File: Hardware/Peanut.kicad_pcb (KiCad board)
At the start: 2 copper layers, 58 x 36 mm, 42 parts, among them J1 Conn_02x04_Odd_Even, J2 Conn_02x04_Odd_Even, SW1 Push_Button, SW2 Push_Button, SW3 Push_Button, SW4 Push_Button, SW5 Slide Switch, U1 BNO085, U2 PCF8574, U3 HDC2010YPAR, U4 LTR-303ALS-01, U5 ADS1115IDGSR, Y1 Crystal_32.768kHz

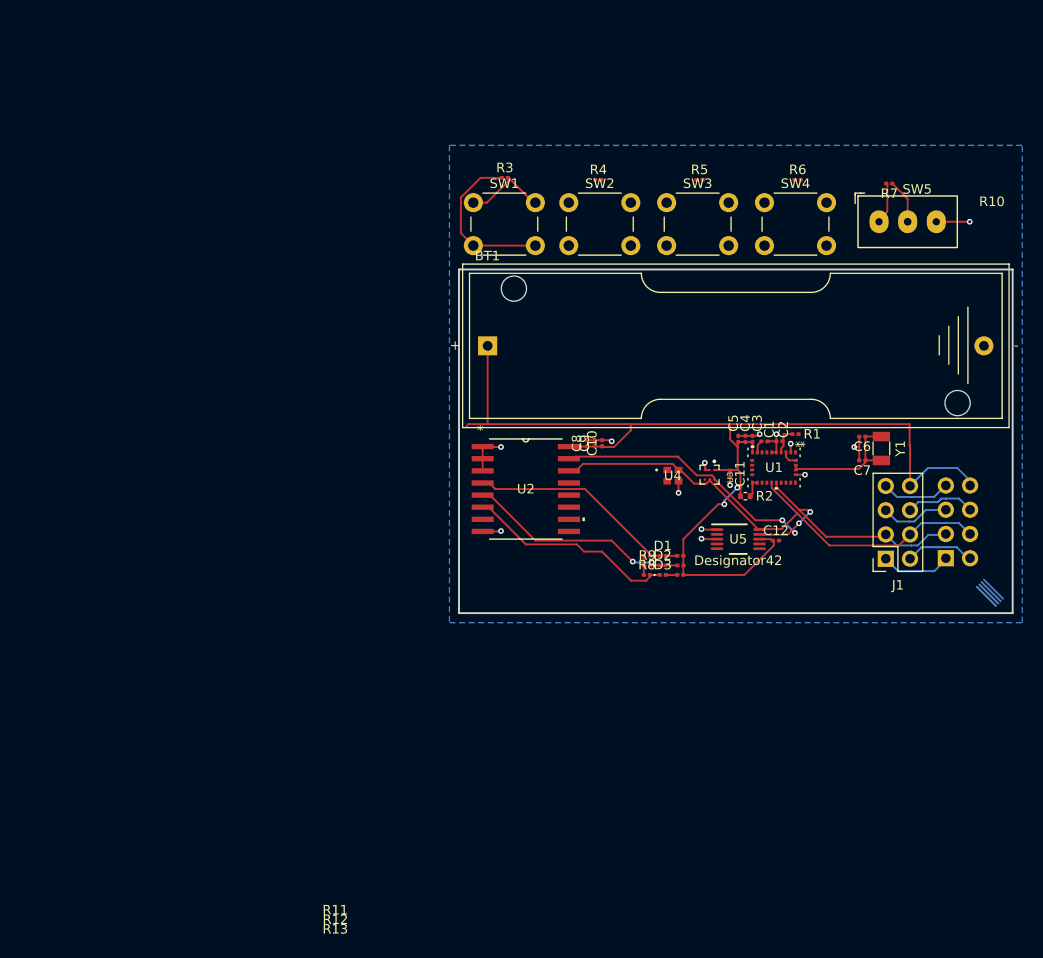
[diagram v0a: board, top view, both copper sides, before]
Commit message: Use Peanut symbols, fix ERC errors, progress on DAC & Pressure
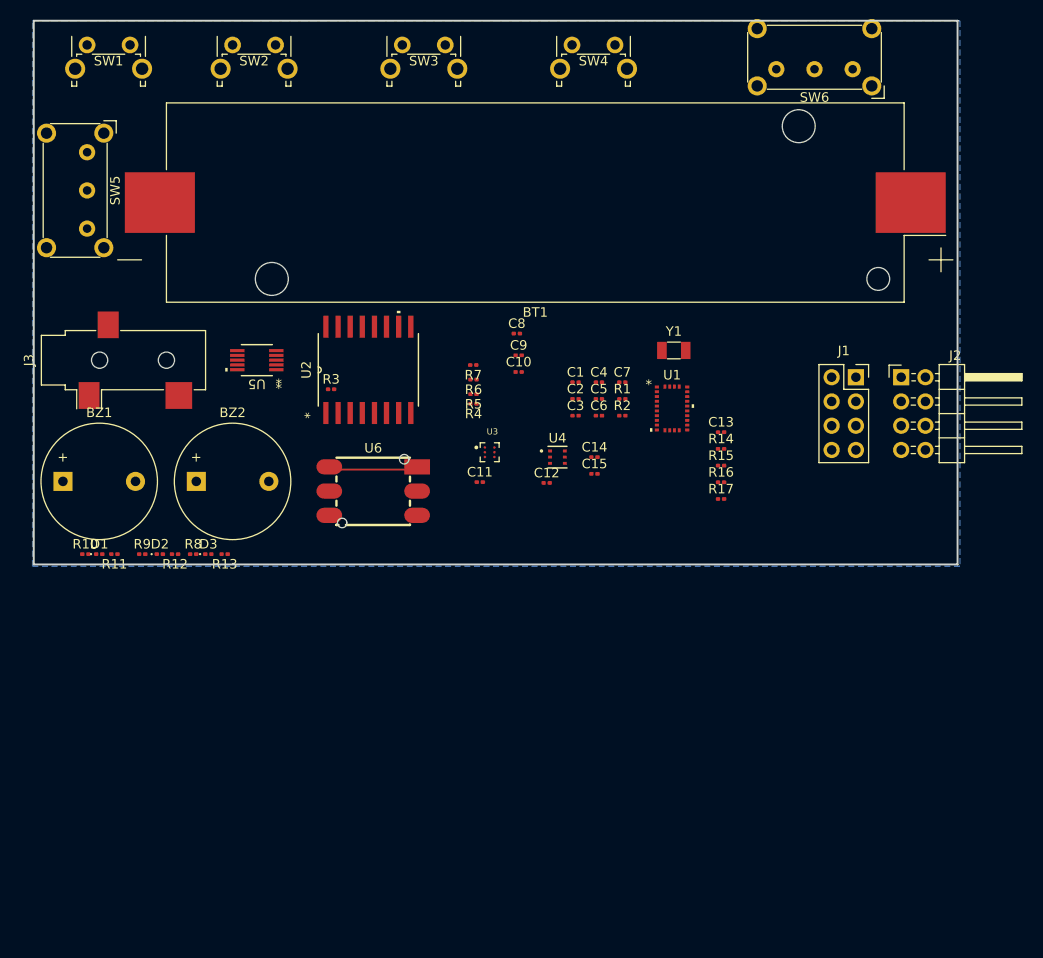
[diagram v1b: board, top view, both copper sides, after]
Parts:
- added BZ1: Buzzer, Buzzer_Beeper:Buzzer_12x9.5RM7.6, F.Cu at (63.5, 76.2)
- added BZ2: Buzzer, Buzzer_Beeper:Buzzer_12x9.5RM7.6, F.Cu at (77.5, 76.2)
- added C13: 0.1uF, Capacitor_SMD:C_0201_0603Metric, F.Cu at (132.5, 71.0)
- added C14: 0.1uF, Capacitor_SMD:C_0201_0603Metric, F.Cu at (119.2, 73.7)
- added C15: 0.1uF, Capacitor_SMD:C_0201_0603Metric, F.Cu at (119.2, 75.4)
- added J3: AudioPlug3, Connector_Audio:Jack_3.5mm_CUI_SJ-3523-SMT_Horizontal, F.Cu at (69.8, 63.5)
- added R14: 1k, Resistor_SMD:R_0201_0603Metric, F.Cu at (132.5, 72.8)
- added R15: 1k, Resistor_SMD:R_0201_0603Metric, F.Cu at (132.5, 74.5)
- added R16: 56k, Resistor_SMD:R_0201_0603Metric, F.Cu at (132.5, 76.3)
- added R17: 56k, Resistor_SMD:R_0201_0603Metric, F.Cu at (132.5, 78.0)
- added SW6: Slide Switch, Button_Switch_THT:SW_E-Switch_EG1224_SPDT_Angled, F.Cu at (146.2, 33.0)
- added U6: LWP040-PSGLC-S, Peanut:SOP-4_L7.0-W7.0-P2.54-LS10.3-TL-CW_LWP040-PSGLC-S, F.Cu at (96.0, 77.2)
- BT1: value Battery -> 3.3V; footprint Battery:BatteryHolder_Keystone_2460_1xAA -> Battery:BatteryHolder_Keystone_1042_1x18650
- J2: moved to F.Cu
- R2: footprint Resistor_SMD:R_0402_1005Metric -> Resistor_SMD:R_0201_0603Metric
- SW1, SW2, SW3, SW4: footprint Button_Switch_THT:SW_PUSH_6mm -> Button_Switch_THT:SW_Tactile_SPST_Angled_PTS645Vx58-2LFS
- SW5: footprint PCM_SL_Devices:Slide_Switch_SPDT_P3mm_10x5x10mm -> Button_Switch_THT:SW_E-Switch_EG1224_SPDT_Angled
- U1: footprint Snapeda:LGA28_5.2X3.8_CEV -> Peanut:LGA28_5.2X3.8_CEV
- U2: footprint Snapeda:DW16 -> Peanut:DW16
- U3: footprint Snapeda:BGA6C100X50P2X3_HDC2010YPAR -> Peanut:HDC2010YPAR
- U4: footprint Snapeda:LTR-329ALS-01_LTO -> Peanut:LTR-308ALS-01_LTO
- U5: value ADS1115IDGSR -> MCP4728T-E/UN; footprint Snapeda:DGS0010A_N -> Peanut:MSOP10_MC_MCH
- moved SW5 83.3 mm to (66.0, 41.7), turned to -90 degrees
- moved R11 59.3 mm to (68.9, 83.8)
- moved D1 59.0 mm to (67.3, 83.8)
- moved R10 58.8 mm to (65.9, 83.8)
- moved U5 53.8 mm to (83.8, 63.5), turned to 180 degrees
- moved R12 53.0 mm to (75.2, 83.8)
- moved R9 52.9 mm to (71.8, 83.8)
- moved D2 52.7 mm to (73.7, 83.8)
- moved R13 47.8 mm to (80.5, 83.8)
- moved D3 47.7 mm to (78.7, 83.8)
- moved R8 47.6 mm to (77.2, 83.8)
- moved R7 47.6 mm to (106.5, 64.0)
- moved SW1 43.7 mm to (66.0, 30.5)
- moved R6 39.9 mm to (106.5, 65.5), turned to 180 degrees
- moved SW2 38.9 mm to (81.3, 30.5)
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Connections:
- BT1 pad 1: +3V3 -> Net-(BT1-+)
- BT1 pad 2: GNDREF -> GND
- C1 pad 2: GNDREF -> GND
- C10 pad 2: GNDREF -> GND
- C11 pad 2: GNDREF -> GND
- C2 pad 1: GNDREF -> GND
- C3 pad 2: GNDREF -> GND
- C4 pad 2: GNDREF -> GND
- C5 pad 2: GNDREF -> GND
- C6 pad 2: GNDREF -> GND
- C7 pad 1: Net-(U1-XIN32) -> Net-(U1-XOUT32/CLKSEL1)
- C7 pad 2: GNDREF -> GND
- C8 pad 2: GNDREF -> GND
- C9 pad 2: GNDREF -> GND
- R3 pad 1: Net-(R3-Pad1) -> +3V3
- R4 pad 1: Net-(R3-Pad1) -> +3V3
- R5 pad 1: Net-(R3-Pad1) -> +3V3
- R6 pad 1: Net-(R3-Pad1) -> +3V3
- R7 pad 1: Net-(R3-Pad1) -> +3V3
- SW1 pad 2: Net-(R3-Pad1) -> +3V3
- SW2 pad 2: Net-(R3-Pad1) -> +3V3
- SW3 pad 2: Net-(R3-Pad1) -> +3V3
- SW4 pad 2: Net-(R3-Pad1) -> +3V3
- SW5 pad 2: Net-(R3-Pad1) -> +3V3
- SW5 pad 3: GNDREF -> GND
- U1 pad 2: GNDREF -> GND
- U1 pad 25: GNDREF -> GND
- U1 pad 26: Net-(U1-XIN32) -> Net-(U1-XOUT32/CLKSEL1)
- U1 pad 5: GNDREF -> GND
- U1 pad 6: GNDREF -> GND
- U2 pad 1: GNDREF -> GND
- U2 pad 2: GNDREF -> GND
- U2 pad 3: GNDREF -> GND
- U2 pad 8: GNDREF -> GND
- U3 pad B1: GNDREF -> GND
- U3 pad C1: GNDREF -> GND
- U4 pad 3: GNDREF -> GND
- U5 pad 1: GNDREF -> +3V3
- U5 pad 10: SCL -> GND
- U5 pad 2: unconnected-(U5-ALERT_RDY-Pad2) -> SCL
- U5 pad 3: GNDREF -> SDA
- U5 pad 4: unconnected-(U5-AIN0-Pad4) -> GND
- U5 pad 6: unconnected-(U5-AIN2-Pad6) -> Net-(U5-VOUTA)
- U5 pad 7: unconnected-(U5-AIN3-Pad7) -> Net-(U5-VOUTB)
- U5 pad 8: +3V3 -> Net-(BZ2-+)
- U5 pad 9: SDA -> Net-(BZ1-+)
- Y1 pad 2: Net-(U1-XIN32) -> Net-(U1-XOUT32/CLKSEL1)
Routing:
- net +3V3: track 119.9 -> 0.00 mm, vias 2 -> 0
- net SDA: track 55.5 -> 0.00 mm, vias 4 -> 0
- net SCL: track 52.9 -> 0.00 mm
- net GNDREF: track 30.3 -> 0.00 mm, vias 14 -> 0
- net Net-(R3-Pad1): track 21.9 -> 0.00 mm
- net Net-(D3-K): track 21.8 -> 0.00 mm
- net Net-(D2-K): track 21.2 -> 0.00 mm, vias 2 -> 0
- net Net-(D1-K): track 21.1 -> 0.00 mm
- net Net-(U1-XIN32): track 14.3 -> 0.00 mm
- net (no net): track 11.3 -> 0.00 mm
- net Net-(U2-P3): track 9.24 -> 0.00 mm
- net Net-(J1-Pin_6): track 7.35 -> 0.00 mm
- net UART_TX: track 7.30 -> 0.00 mm
- net UART_RX: track 7.28 -> 0.00 mm
- net Net-(J1-Pin_5): track 7.08 -> 0.00 mm
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- added copper zone on B.Cu, net GND
- removed copper zone on B.Cu, net GNDREF
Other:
- board size 58 x 36 mm -> 96.8 x 57 mm

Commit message: Fully wired board!
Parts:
- removed D3: BLU, LED_SMD:LED_0201_0603Metric
- removed R13: 2.2k, Resistor_SMD:R_0201_0603Metric
- removed R16, R17: 56k, Resistor_SMD:R_0201_0603Metric
- removed R8: 100k, Resistor_SMD:R_0201_0603Metric
- added C16: 0.1uF, Resistor_SMD:R_01005_0402Metric, F.Cu at (156.5, 86.0)
- added C17: 0.1uF, Resistor_SMD:R_01005_0402Metric, F.Cu at (164.0, 86.0)
- added Q1: Q_NPN_BEC, Package_TO_SOT_SMD:SOT-23-3, F.Cu at (167.5, 78.0)
- added U7: ADS1015IDGSR, Package_SO:VSSOP-10_3x3mm_P0.5mm, F.Cu at (160.0, 85.5)
- added U8: INA350ABSIDDFR, Package_TO_SOT_SMD:TSOT-23-8, F.Cu at (154.0, 86.5)
- C1, C10, C11, C12, C14, C15, C2, C3, C4, C5, C8, C9: footprint Capacitor_SMD:C_0201_0603Metric -> Resistor_SMD:R_01005_0402Metric
- C13: value 0.1uF -> 1uF; footprint Capacitor_SMD:C_0201_0603Metric -> Resistor_SMD:R_01005_0402Metric
- J2: footprint Connector_PinHeader_2.54mm:PinHeader_2x04_P2.54mm_Horizontal -> Peanut:PinHeader_2x04_P2.54mm_Horizontal_Flipped; moved to B.Cu
- R1, R10, R11, R12, R2, R3, R4, R5, R6, R7, R9: footprint Resistor_SMD:R_0201_0603Metric -> Resistor_SMD:R_0402_1005Metric
- R14, R15: value 1k -> R; footprint Resistor_SMD:R_0201_0603Metric -> Resistor_SMD:R_0402_1005Metric
- SW5, SW6: footprint Button_Switch_THT:SW_E-Switch_EG1224_SPDT_Angled -> Peanut:SW-TH_SK12D07VG4
- U2: value PCF8574 -> PCF8574APWR; footprint Peanut:DW16 -> Peanut:PW20
- moved U2 71.2 mm to (165.0, 49.0), turned to 180 degrees
- moved C10 59.8 mm to (169.7, 52.0)
- moved C9 59.8 mm to (169.7, 50.5)
- moved C8 59.7 mm to (169.7, 49.5)
- moved BZ1 56.4 mm to (119.7, 81.0)
- moved BZ2 55.4 mm to (132.7, 81.0)
- moved U6 51.7 mm to (147.5, 82.0), turned to 90 degrees
- moved C11 49.1 mm to (146.3, 46.5), turned to 180 degrees
- moved R6 46.6 mm to (149.5, 47.5), turned to 90 degrees
- moved U3 45.7 mm to (147.0, 49.0)
- moved SW1 45.3 mm to (107.7, 48.2)
- moved SW2 45.1 mm to (122.7, 48.2)
- moved C6 44.0 mm to (163.2, 76.2), turned to 180 degrees
- moved C7 43.9 mm to (163.2, 81.2), turned to 180 degrees
- moved C1 43.6 mm to (159.5, 76.2)
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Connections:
- C13 pad 1: GND -> +3V3
- C13 pad 2: /Pressure and ADC/PRESSURE -> GND
- R14 pad 1: Net-(U6-VOUT+) -> Net-(Q1-E)
- R14 pad 2: Net-(U7--) -> Net-(U7-AIN3)
- R15 pad 1: Net-(U7-+) -> Net-(U7-AIN3)
- R15 pad 2: Net-(U6-VOUT-) -> GND
- R3 pad 2: Net-(U2-P3) -> Net-(U2-P4)
- R4 pad 2: Net-(U2-P4) -> Net-(U2-P3)
- R5 pad 2: Net-(U2-P5) -> Net-(U2-P1)
- R6 pad 2: Net-(U2-P6) -> Net-(U2-P2)
- R7 pad 2: Net-(U2-P7) -> Net-(U2-P5)
- SW1 pad 1: Net-(U2-P3) -> Net-(U2-P4)
- SW2 pad 1: Net-(U2-P4) -> Net-(U2-P3)
- SW3 pad 1: Net-(U2-P5) -> Net-(U2-P1)
- SW4 pad 1: Net-(U2-P6) -> +3V3
- SW4 pad 2: +3V3 -> Net-(U2-P2)
- SW5 pad 1: Net-(U2-P7) -> Net-(U2-P5)
- U1 pad 17: /Motion Sensor/I2CADDR -> GND
- U2 pad 1: GND -> /DigitalMuxer/~{INT}
- U2 pad 10: Net-(U2-P5) -> /DigitalMuxer/P2
- U2 pad 11: Net-(U2-P6) -> Net-(U2-P1)
- U2 pad 12: Net-(U2-P7) -> Net-(U2-P2)
- U2 pad 13: /DigitalMuxer/Reset pin -> unconnected-(U2-NC-Pad13)
- U2 pad 14: SCL -> Net-(U2-P3)
- U2 pad 15: SDA -> GND
- U2 pad 16: +3V3 -> Net-(U2-P4)
- U2 pad 2: GND -> SCL
- U2 pad 3: GND -> unconnected-(U2-NC-Pad3)
- U2 pad 4: Net-(D1-K) -> SDA
- U2 pad 5: Net-(D2-K) -> +3V3
- U2 pad 6: Net-(D3-K) -> GND
- U2 pad 7: Net-(U2-P3) -> GND
- U2 pad 8: GND -> unconnected-(U2-NC-Pad8)
- U2 pad 9: Net-(U2-P4) -> GND
- U5 pad 5: unconnected-(U5-RDY/~{BSY}-Pad5) -> /DAC and Sound/RDY/~{BSY}
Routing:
- net +3V3: track 0.00 -> 320.3 mm, vias 0 -> 8
- net SCL: track 0.00 -> 180.2 mm, vias 0 -> 6
- net SDA: track 0.00 -> 179.0 mm, vias 0 -> 8
- net Net-(D1-K): track 0.00 -> 96.1 mm, vias 0 -> 2
- net GND: track 9.63 -> 100.2 mm, vias 0 -> 20
- net Net-(D2-K): track 0.00 -> 89.3 mm, vias 0 -> 2
- net Net-(U2-P5): track 0.00 -> 76.8 mm, vias 0 -> 1
- net Net-(U2-P4): track 0.00 -> 67.7 mm, vias 0 -> 2
- net Net-(U2-P3): track 0.00 -> 52.0 mm
- net /DigitalMuxer/P2: track 0.00 -> 34.1 mm, vias 0 -> 2
- net Net-(U2-P1): track 0.00 -> 31.9 mm, vias 0 -> 2
- net Net-(BZ2-+): track 0.00 -> 21.0 mm
- net Net-(BT1-+): track 0.00 -> 16.9 mm
- net Net-(U2-P2): track 0.00 -> 14.7 mm
- net Net-(U5-VOUTA): track 0.00 -> 14.0 mm
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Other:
- board size 96.8 x 57 mm -> 92 x 44 mm

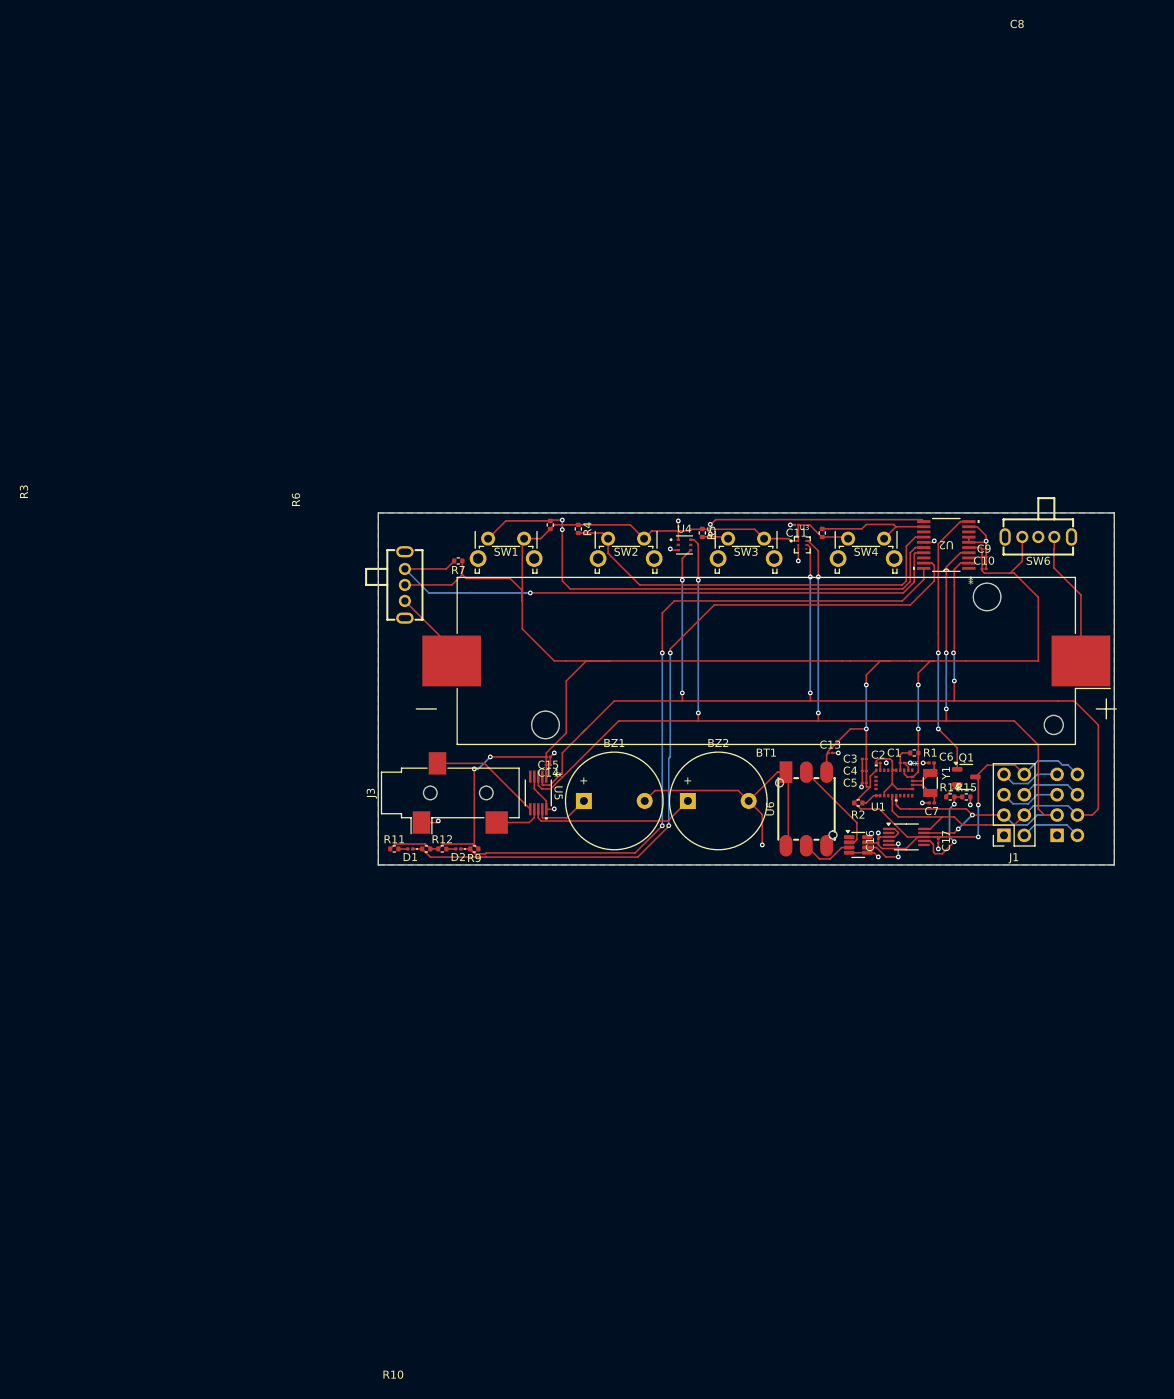
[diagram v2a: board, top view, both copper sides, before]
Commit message: Initial OS architecture, and updated PCB work After a joint planning session, designed and architected OS structure: ``` src/ |- os: Audio, Accelerometer, Humidity, etc |- drivers: I2C interfaces, per-chip ```
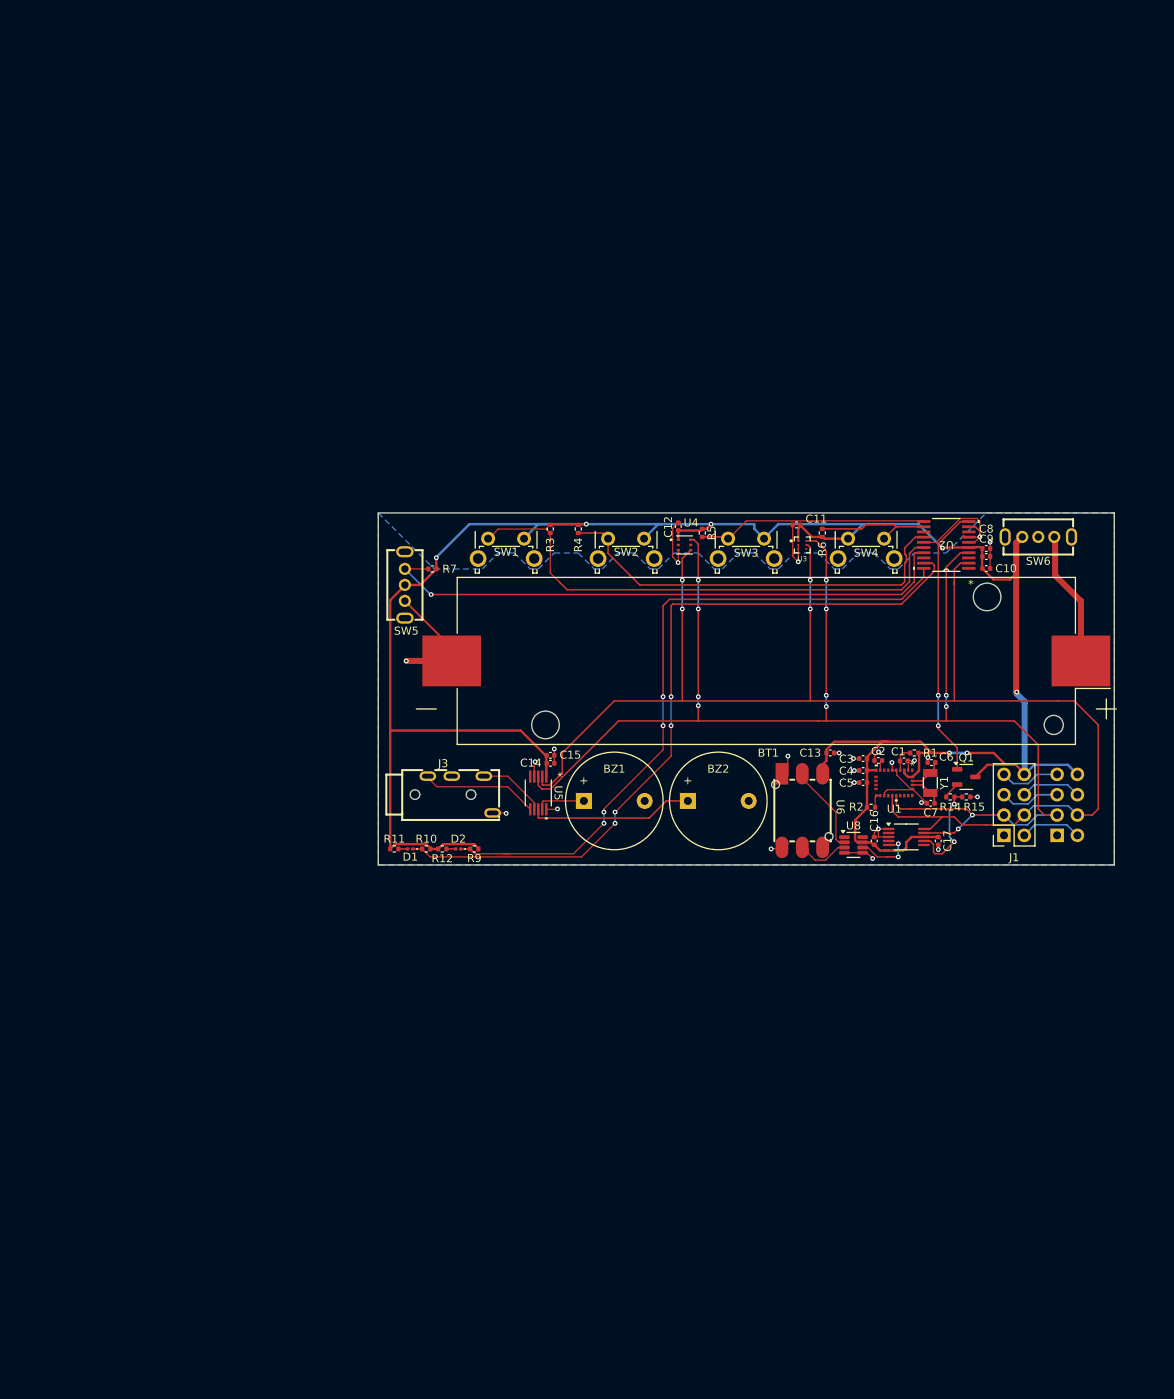
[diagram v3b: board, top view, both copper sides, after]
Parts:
- C1, C10, C11, C12, C13, C16, C17, C2, C3, C4, C5, C8, C9: footprint Resistor_SMD:R_01005_0402Metric -> Capacitor_SMD:C_0402_1005Metric
- C14, C15: value 0.1uF -> 100nF; footprint Resistor_SMD:R_01005_0402Metric -> Capacitor_SMD:C_0402_1005Metric
- C6, C7: footprint Capacitor_SMD:C_0201_0603Metric -> Capacitor_SMD:C_0402_1005Metric
- J1: value Conn_02x04_Odd_Even -> BL602 Female JST Connector
- J2: value Conn_02x04_Odd_Even -> Extension Male JST Connector
- J3: footprint Connector_Audio:Jack_3.5mm_CUI_SJ-3523-SMT_Horizontal -> Peanut:AUDIO-TH_PJ-320A-4P-DIP
- moved R7 3.39 mm to (100.8, 52.0)
- moved R2 1.70 mm to (155.6, 81.8)
- moved J3 1.26 mm to (104.2, 80.2), turned to 0 degrees
- moved U8 0.60 mm to (153.4, 86.5)
- moved U6 0.54 mm to (147.0, 82.2)
- moved C16 0.50 mm to (156.0, 86.0)
- moved R3 0.50 mm to (115.5, 47.0), turned to -90 degrees
- moved C14 0.34 mm to (115.5, 76.3)
- moved C15 0.34 mm to (115.5, 75.3)
- moved C1 0.32 mm to (159.7, 76.0)
- moved C12 0.30 mm to (131.5, 46.7)
- moved C2 0.30 mm to (156.5, 76.0)
- moved C10 0.28 mm to (170.0, 52.0)
- moved C8 0.28 mm to (170.0, 49.5)
- moved C9 0.28 mm to (170.0, 50.5)
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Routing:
- net +3V3: track 320.3 -> 294.0 mm, vias 8 -> 7
- net GND: track 100.2 -> 94.1 mm, vias 20 -> 24
- net Net-(U2-P5): track 76.8 -> 73.1 mm
- net Net-(U2-P1): track 31.9 -> 28.7 mm, vias 2 -> 0
- net Net-(D2-K): track 89.3 -> 86.1 mm, vias 2 -> 4
- net Net-(U5-VOUTB): track 5.99 -> 8.27 mm
- net Net-(U2-P4): track 67.7 -> 65.6 mm, vias 2 -> 0
- net Net-(D1-K): track 96.1 -> 94.5 mm, vias 2 -> 4
- net Net-(BZ1-+): track 7.11 -> 6.07 mm
- net Net-(U7-AIN1): track 7.26 -> 8.21 mm
- net SCL: track 180.2 -> 179.3 mm, vias 6 -> 4
- net Net-(U6-VOUT-): track 6.64 -> 7.41 mm
- net Net-(U1-S_SCL): track 2.63 -> 1.94 mm
- net Net-(U5-VOUTA): track 14.0 -> 14.6 mm
- net SDA: track 179.0 -> 179.4 mm, vias 8 -> 12
